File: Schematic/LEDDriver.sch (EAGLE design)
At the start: 35 parts, among them IC1 LM324N, IC2 LM317, IC3 75176AP, IC4 LM317

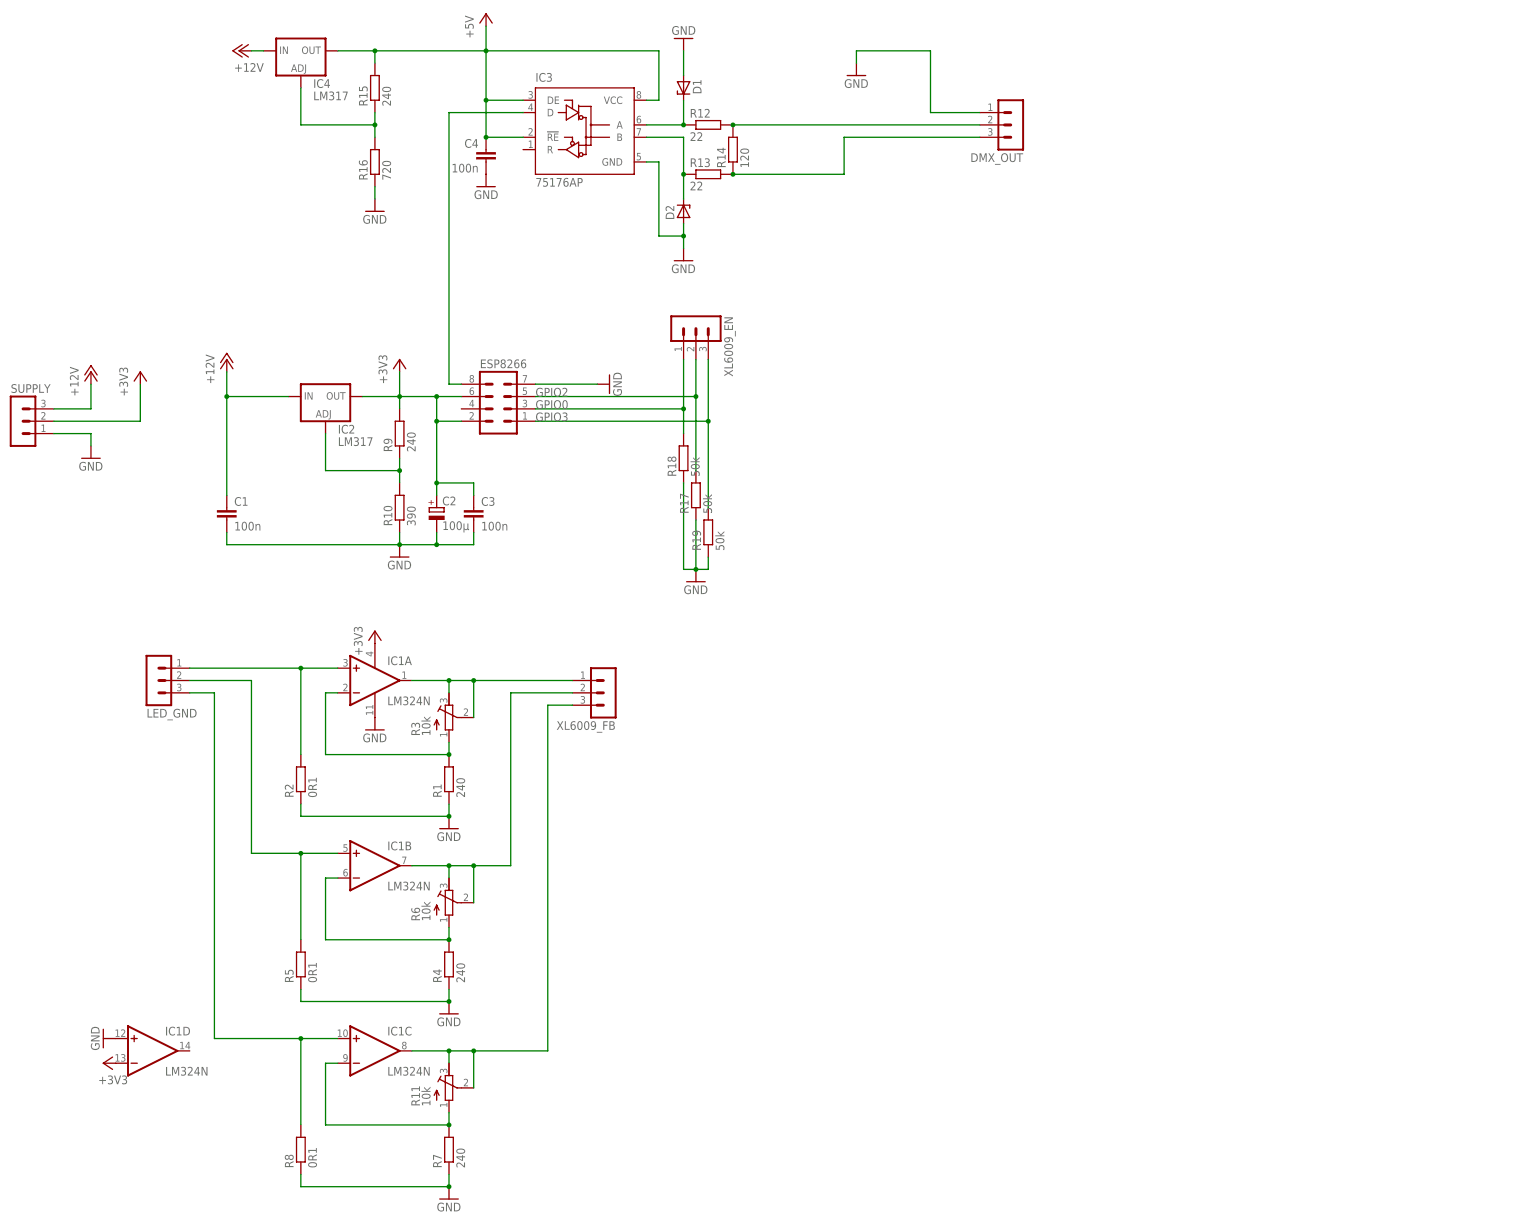
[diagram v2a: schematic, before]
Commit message: Switch OpAmp of, if all LEDs are off
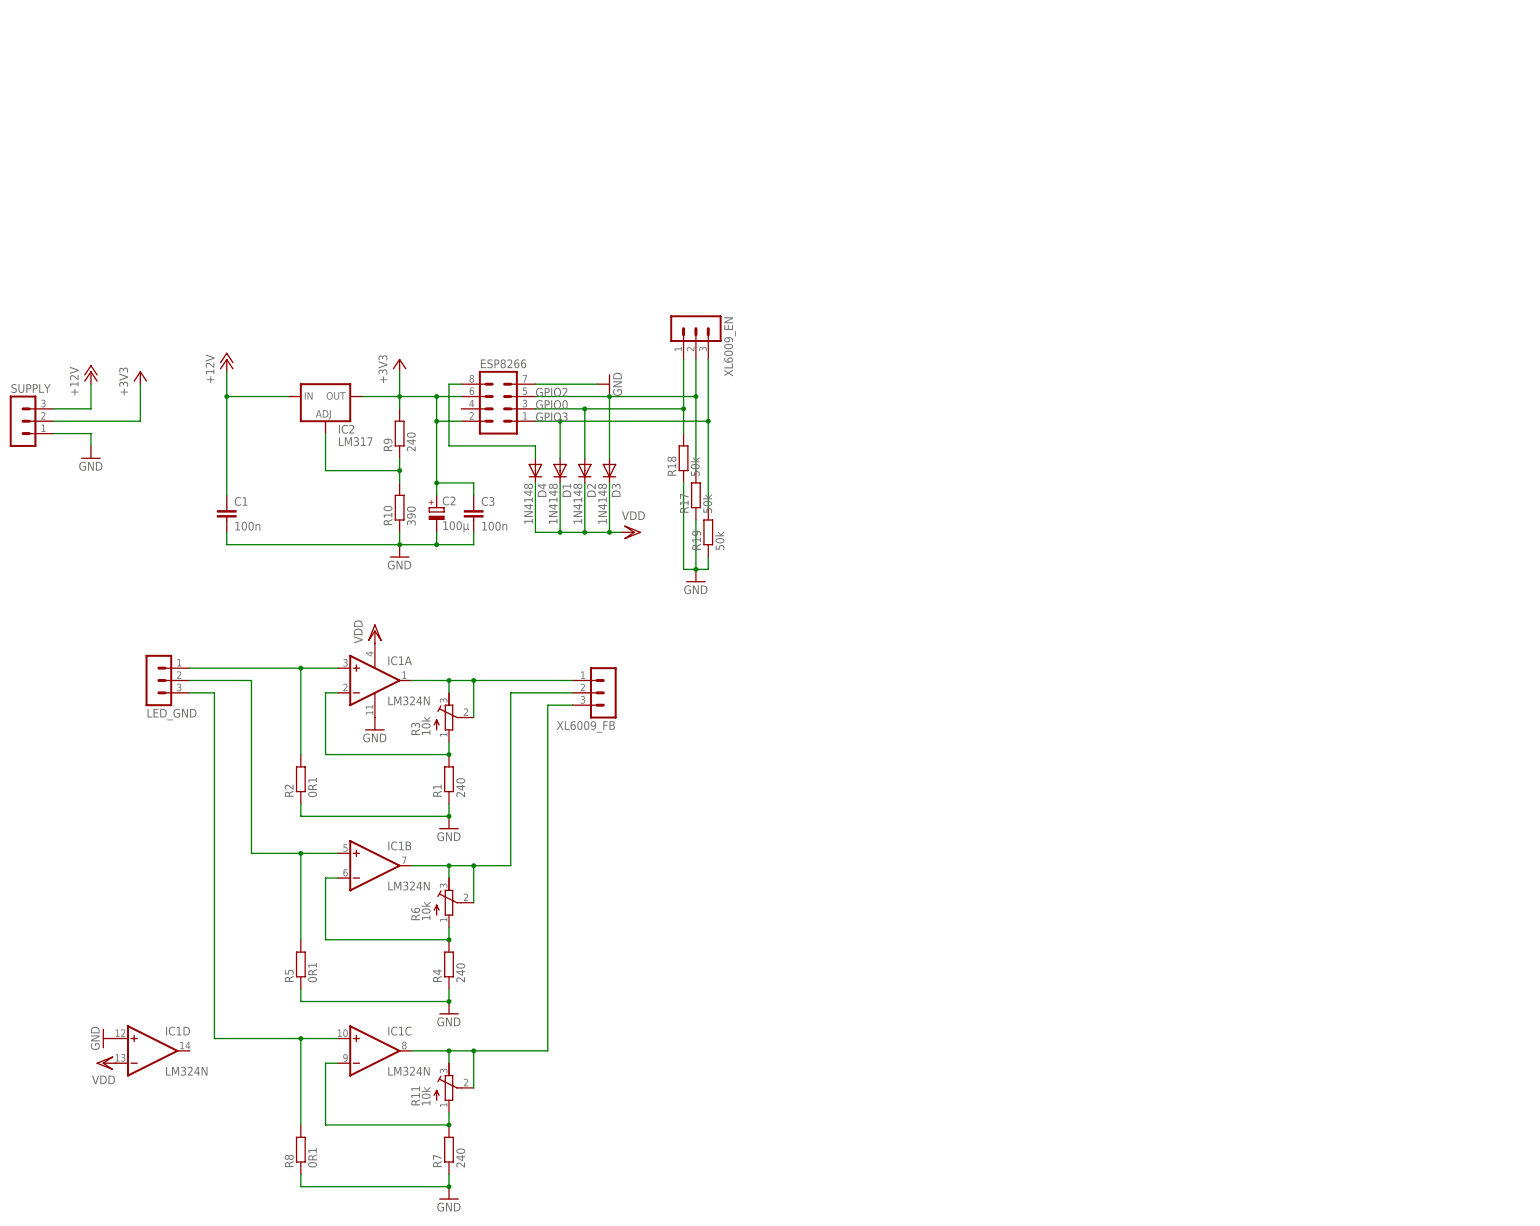
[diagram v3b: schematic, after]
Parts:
- removed C4: 100n, rcl:C-EU075-032X103
- removed DMX_OUT: (no value), con-lstb:MA03-1
- removed IC3: 75176AP, 751xx:75176AP
- removed IC4: LM317, v-reg:LM317TS
- removed R12, R13: 22, rcl:R-EU_0204/2V
- removed R14: 120, rcl:R-EU_0204/2V
- removed R15: 240, rcl:R-EU_0204/2V
- removed R16: 720, rcl:R-EU_0207/10
- added D3, D4: 1N4148, diode:DIODE-D-2.5
- D1: value (none) -> 1N4148; device diode:ZENER-DIODEZD-2.5 -> diode:DIODE-D-2.5
- D2: value (none) -> 1N4148; device diode:ZENER-DIODEDO34-7 -> diode:DIODE-D-2.5
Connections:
- removed net +5V: C4.1, IC3.!RE, IC3.DE, IC3.VCC, IC4.OUT, R15.2
- removed net DMX2: DMX_OUT.2, R12.2, R14.2
- removed net N$1: ESP8266.8, IC3.D
- removed net N$14: D1.C, IC3.A, R12.1
- removed net N$15: D2.C, IC3.B, R13.1
- removed net N$16: DMX_OUT.3, R13.2, R14.1
- removed net N$8: IC4.ADJ, R15.1, R16.2
- new net N$23: D4.A, ESP8266.8
- new net VDD: D1.C, D2.C, D3.C, D4.C, IC1D.-IN, IC1P.V+
- net +12V: no longer IC4.IN
- net +3V3: no longer IC1D.-IN, IC1P.V+
- net GND: no longer C4.2, D1.A, D2.A, DMX_OUT.1, IC3.GND, R16.1
- net GPIO0: now also D2.A
- net GPIO2: now also D3.A
- net GPIO3: now also D1.A
